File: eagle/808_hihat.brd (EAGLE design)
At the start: 100 x 80 mm, 101 parts, among them IC1 TL072P, IC2 TL072P, Q1 2N3904, Q10 2N3904, Q11 2N3904, Q12 2N3904, Q13 2N3906, Q14 2N3906, Q2 2N3904, Q3 2N3904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

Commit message: board with drc
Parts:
- moved CH_OUT_NORM 172.9 mm to (92.7, 22.9), turned to 180 degrees
- moved U$2 141.5 mm to (87.6, 72.4), turned to 180 degrees
- moved DIGI_NOISE 133.1 mm to (38.1, 67.3)
- moved R172* 131.1 mm to (85.1, 15.2), turned to 270 degrees
- moved OH_OUT_NORM 123.5 mm to (55.9, 22.9), turned to 180 degrees
- moved R169* 93.4 mm to (48.3, 17.8), turned to 270 degrees
- moved U$1 34.5 mm to (6.35, 43.2), turned to 270 degrees

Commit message: beginning manual layout
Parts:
- removed IC2: TL072P, linear:DIL08
- added IC3: TL071P, 808_lt:DIL08
- moved R16* 175.7 mm to (77.5, 59.7), turned to 180 degrees
- moved Q12 175.0 mm to (76.2, 49.5)
- moved Q5 158.1 mm to (66.0, 47.0), turned to 270 degrees
- moved R11* 157.9 mm to (81.3, 53.3), turned to 90 degrees
- moved R13* 156.9 mm to (64.8, 52.1)
- moved R138* 156.8 mm to (66.0, 40.6), turned to 90 degrees
- moved CH_TRIG 155.9 mm to (67.3, 62.2)
- moved Q6 153.0 mm to (45.7, 43.2), turned to 180 degrees
- moved R139* 146.5 mm to (45.7, 35.6)
- moved CH_ACCENT 146.0 mm to (77.5, 62.2)
- moved C62* 142.4 mm to (40.6, 31.8)
- moved R7* 128.5 mm to (67.3, 57.1), turned to 90 degrees
- moved R2* 124.3 mm to (71.1, 59.7), turned to 90 degrees
- moved R137* 122.3 mm to (39.4, 38.1), turned to 270 degrees
- moved R55*1 121.8 mm to (21.6, 74.9)
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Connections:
- removed net V+: IC1.8, IC2.8
- removed net V-: IC1.4, IC2.4
- net +12V: now also IC1.8, IC3.7
- net -12V: now also IC1.4, IC3.4
- net GND: now also IC3.3; no longer IC2.3
- net N$4: now also IC3.2; no longer IC2.2
- net TO_HH: now also IC3.6; no longer IC2.1

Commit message: parts on the board
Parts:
- R147*: device TR808clone:0207/2V -> TR808clone:0207/7
- R161*: device TR808clone:0207/5V -> TR808clone:0207/2V
- moved C83* 177.4 mm to (80.0, 12.7), turned to 90 degrees
- moved R162* 171.3 mm to (68.6, 36.8), turned to 270 degrees
- moved R161* 171.0 mm to (76.2, 33.0), turned to 180 degrees
- moved R158* 156.1 mm to (82.5, 19.1), turned to 270 degrees
- moved R159* 155.1 mm to (69.8, 12.7), turned to 180 degrees
- moved R160* 153.8 mm to (66.0, 29.2)
- moved C69* 151.7 mm to (49.5, 54.6)
- moved C81* 150.6 mm to (66.0, 21.6)
- moved C68* 147.3 mm to (52.1, 40.6), turned to 270 degrees
- moved R157* 145.0 mm to (83.8, 30.5), turned to 270 degrees
- moved IC3 144.4 mm to (22.9, 66.0), turned to 180 degrees
- moved C66* 139.8 mm to (50.8, 45.7)
- moved R152* 136.4 mm to (38.1, 59.7), turned to 90 degrees
- moved R146* 133.0 mm to (55.9, 31.8)
- moved C82* 132.8 mm to (76.2, 29.2), turned to 180 degrees
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
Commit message: 93pct ar
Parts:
- C15*1, C68*: device TR808clone:C035-025X75 -> TR808clone:C050-024X044
- C67*: device TR808clone:C035-030X60 -> TR808clone:C050-024X044
- C74*: device TR808clone:C035-025X75 -> TR808clone:C050-025X075
- D13*, D14*: value 1N4148DO35-7 -> 1N4148DO35-10; device TR808clone:DO35-7 -> TR808clone:DO35-10
- R1*, R159*: device TR808clone:0207/5V -> TR808clone:0207/2V
- R11*, R12*, R133*, R134*, R142*, R145*, R146*, R156*, R162*, R169*, R172*: device TR808clone:0207/5V -> TR808clone:0207/7
- R59*1: device TR808clone:0207/2V -> TR808clone:0207/5V
- moved U$2 25.4 mm to (63.5, 72.4), turned to 0 degrees
- moved C81* 24.1 mm to (43.2, 14.0), turned to 90 degrees
- moved R143* 20.3 mm to (44.5, 47.0)
- moved R150* 19.7 mm to (24.1, 57.1)
- moved C60* 19.4 mm to (8.89, 15.2), turned to 180 degrees
- moved Q10 15.9 mm to (10.2, 24.1)
- moved U$1 14.0 mm to (7.62, 49.5), turned to 270 degrees
- moved R153* 13.1 mm to (66.0, 61.0), turned to 0 degrees
- moved D14* 12.6 mm to (49.5, 63.5)
- moved R16* 11.7 mm to (95.2, 53.3), turned to 90 degrees
- moved R133* 11.4 mm to (16.5, 19.1)
- moved Q8 10.9 mm to (21.6, 21.6)
- moved R130* 10.9 mm to (25.4, 33.0), turned to 270 degrees
- moved R17* 10.9 mm to (15.2, 31.8)
- moved R139* 10.5 mm to (43.2, 25.4), turned to 270 degrees
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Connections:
- removed net +5V: U$1.11, U$1.12, U$2.11, U$2.12
- net N$4: now also C15*1.1; no longer C15*1.P$1
- net N$5: now also C15*1.2; no longer C15*1.P$2
- net N$586: now also C67*.2; no longer C67*.P$2
- net N$589: now also C68*.1; no longer C68*.P$1
- net N$591: now also C68*.2; no longer C68*.P$2
- net N$595: now also C74*.2; no longer C74*.P$2
- net N$608: now also C74*.1; no longer C74*.P$1
- net TO_HH: now also C67*.1; no longer C67*.P$1

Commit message: 94pct ar
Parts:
- R130*, R140*, R173*: device TR808clone:0207/5V -> TR808clone:0207/7
- R145*, R162*: device TR808clone:0207/7 -> TR808clone:0207/5V
- moved C60* 15.3 mm to (10.2, 30.5), turned to 0 degrees
- moved R133* 6.48 mm to (10.2, 17.8), turned to 180 degrees
- moved R134* 5.68 mm to (29.2, 24.1), turned to 0 degrees
- moved Q8 4.02 mm to (20.3, 17.8)
- moved R162* 2.84 mm to (76.2, 38.1), turned to 0 degrees
- moved C83* 2.54 mm to (68.6, 15.2)
- moved Q9 2.54 mm to (27.9, 17.8)
- moved R156* 1.27 mm to (69.8, 35.6)
- moved R131* 1.27 mm to (20.3, 26.7), turned to 180 degrees
- moved R132* 1.27 mm to (16.5, 11.4)
- turned Q10 to 180 degrees

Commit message: 94pct6 ar
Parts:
- added C71*1, C71*2: 100n, TR808clone:C030-025X75
- C64*, C66*, C72*, C73*: device TR808clone:C035-025X75 -> TR808clone:C050-024X044
- C81*: device TR808clone:E2-5 -> TR808clone:E3,5-8
- R135*, R155*, R158*, R162*: device TR808clone:0207/5V -> TR808clone:0207/7
- R136*: device TR808clone:0207/5V -> TR808clone:0207/2V
- R156*, R172*: device TR808clone:0207/7 -> TR808clone:0207/5V
- moved R173* 60.1 mm to (24.8, 13.3), turned to 90 degrees
- moved C74* 7.73 mm to (76.2, 47.0), turned to 270 degrees
- moved R154* 6.84 mm to (72.4, 50.8), turned to 270 degrees
- moved R16* 6.84 mm to (92.7, 59.7), turned to 180 degrees
- moved R135* 6.35 mm to (33.0, 35.6), turned to 180 degrees
- moved R143* 5.68 mm to (39.4, 44.5)
- moved R162* 5.68 mm to (81.3, 40.6), turned to 270 degrees
- moved CH_OUT_NORM 5.08 mm to (95.2, 30.5)
- moved C80* 4.58 mm to (62.2, 30.5)
- moved C65* 4.58 mm to (45.7, 54.6)
- moved R142* 4.58 mm to (80.0, 52.1)
- moved C72* 4.58 mm to (61.0, 62.2), turned to 270 degrees
- moved R145* 4.02 mm to (31.8, 43.2)
- moved C81* 4.02 mm to (47.0, 12.7)
- moved R172* 4.02 mm to (94.0, 20.3)
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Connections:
- net +12V: now also C71*1.P$1
- net -12V: now also C71*2.P$2
- net GND: now also C64*.2, C71*1.P$2, C71*2.P$1; no longer C64*.P$2
- net N$219: now also C64*.1, C66*.1; no longer C64*.P$1, C66*.P$1
- net N$220: now also C72*.1; no longer C72*.P$1
- net N$589: now also C66*.2; no longer C66*.P$2
- net N$590: now also C72*.2, C73*.1; no longer C72*.P$2, C73*.P$1
- net N$592: now also C73*.2; no longer C73*.P$2

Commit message: 94pct6 ar
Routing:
- net GND: track 0.00 -> 484.9 mm
- net +12V: track 0.00 -> 195.1 mm
- net N$581: track 0.00 -> 145.7 mm
- net -12V: track 0.00 -> 128.0 mm
- net N$603: track 0.00 -> 81.5 mm
- net N$598: track 0.00 -> 73.3 mm
- net .: track 0.00 -> 43.1 mm
- net N$220: track 0.00 -> 36.9 mm
- net N$17: track 0.00 -> 32.0 mm
- net N$600: track 0.00 -> 28.9 mm
- net N$601: track 0.00 -> 26.6 mm
- net N$573: track 0.00 -> 25.8 mm
- net TO_HH: track 0.00 -> 22.8 mm
- net N$576: track 0.00 -> 22.4 mm
- net N$588: track 0.00 -> 21.6 mm
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
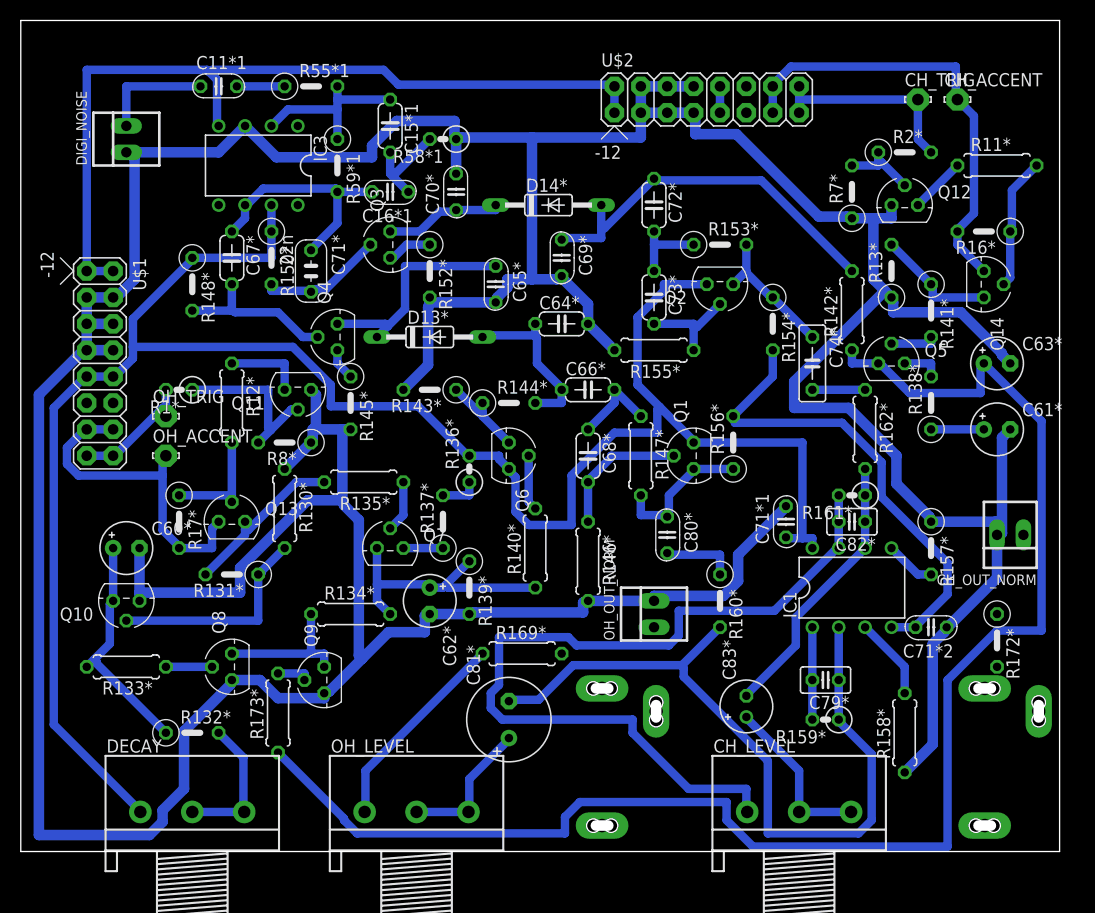
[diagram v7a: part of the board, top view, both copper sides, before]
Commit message: rotated output amp looks promising
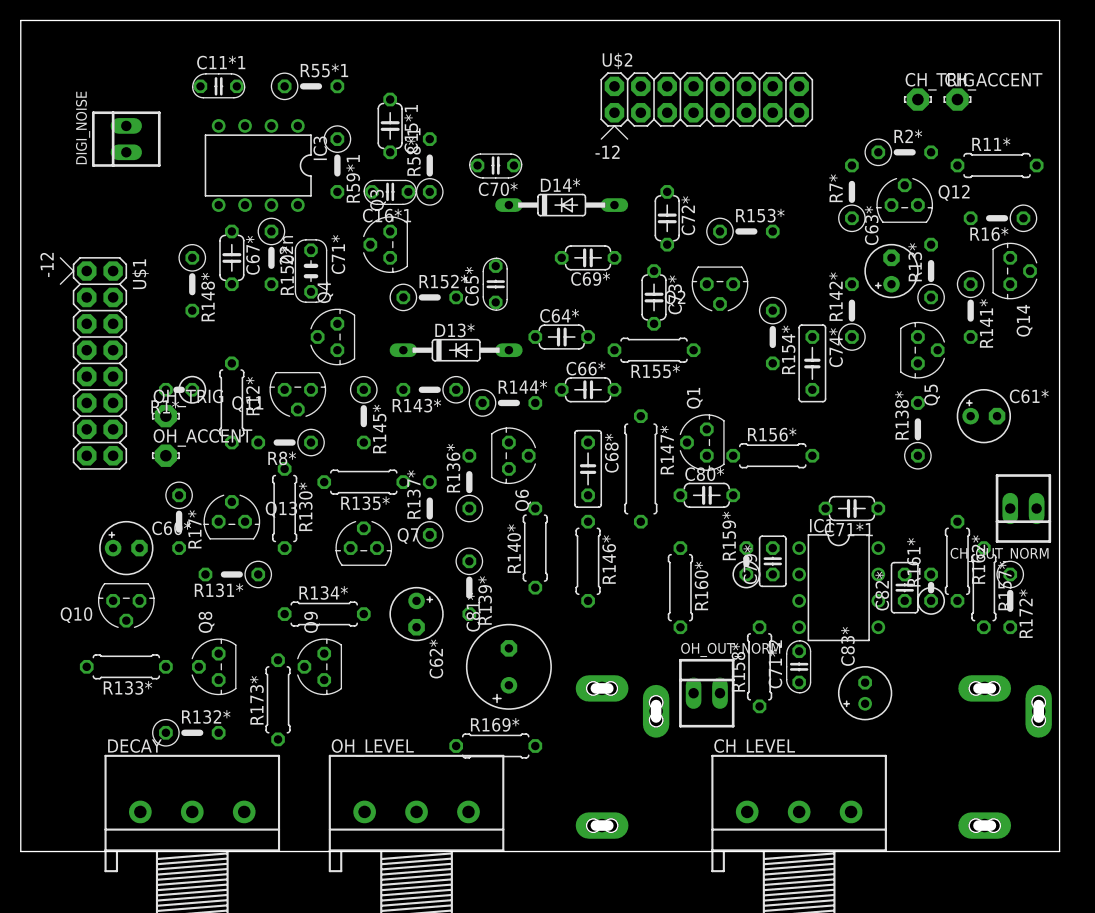
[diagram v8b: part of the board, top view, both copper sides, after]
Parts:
- C68*: device TR808clone:C050-024X044 -> TR808clone:C050-025X075
- C69*, C80*: device TR808clone:C035-025X75 -> TR808clone:C050-024X044
- C71*1: device TR808clone:C030-025X75 -> TR808clone:C050-024X044
- R136*, R58*1: device TR808clone:0207/2V -> TR808clone:0207/5V
- R142*: device TR808clone:0207/7 -> TR808clone:0207/5V
- R147*: device TR808clone:0207/7 -> TR808clone:0309/10
- R156*, R157*, R160*: device TR808clone:0207/5V -> TR808clone:0207/7
- moved R159* 17.0 mm to (69.8, 27.9), turned to 90 degrees
- moved R162* 15.5 mm to (90.2, 27.9)
- moved R158* 15.3 mm to (71.1, 17.8)
- moved C63* 13.5 mm to (83.8, 55.9), turned to 90 degrees
- moved C71*2 13.3 mm to (74.9, 17.8), turned to 90 degrees
- moved C79* 12.5 mm to (72.4, 27.9), turned to 90 degrees
- moved R161* 11.7 mm to (87.6, 25.4), turned to 90 degrees
- moved C83* 11.5 mm to (81.3, 15.2)
- moved R169* 9.25 mm to (45.7, 10.2)
- moved OH_OUT_NORM 9.16 mm to (66.0, 15.2), turned to 0 degrees
- moved C82* 8.13 mm to (85.1, 25.4), turned to 90 degrees
- moved C71*1 6.48 mm to (80.0, 33.0), turned to 180 degrees
- moved R157* 6.35 mm to (92.7, 25.4)
- moved C80* 5.39 mm to (66.0, 34.3), turned to 0 degrees
- moved C81* 5.08 mm to (47.0, 17.8)
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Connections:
- net +12V: now also C71*1.1; no longer C71*1.P$1
- net GND: now also C69*.2, C71*1.2; no longer C69*.P$2, C71*1.P$2
- net N$220: now also C69*.1; no longer C69*.P$1
- net N$597: now also C80*.2; no longer C80*.P$2
- net N$607: now also C80*.1; no longer C80*.P$1
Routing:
- net GND: track 484.9 -> 0.00 mm
- net +12V: track 195.1 -> 0.00 mm
- net N$581: track 145.7 -> 0.00 mm
- net -12V: track 128.0 -> 0.00 mm
- net N$603: track 81.5 -> 0.00 mm
- net N$598: track 73.3 -> 0.00 mm
- net .: track 43.1 -> 0.00 mm
- net N$220: track 36.9 -> 0.00 mm
- net N$17: track 32.0 -> 0.00 mm
- net N$600: track 28.9 -> 0.00 mm
- net N$601: track 26.6 -> 0.00 mm
- net N$573: track 25.8 -> 0.00 mm
- net TO_HH: track 22.8 -> 0.00 mm
- net N$576: track 22.4 -> 0.00 mm
- net N$588: track 21.6 -> 0.00 mm
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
